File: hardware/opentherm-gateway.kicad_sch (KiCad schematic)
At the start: 83 parts, among them J1 BOILER, J2 THERM, J3 USB-C, J5 5V IN, J6 NTC, Q1 MMBT2907A, Q2 MMBT2907A, Q3 MMBT2907A, Q4 MMBT2907A, Q5 MMBT2222A, Q6 MMBT2222A, SW1 RESET, SW2 BOOT, U1 MT3540-F23, U2 LTV-817S, U3 LTV-817S, U4 ESP32-C3-WROOM-02-N4, U5 AP2112K-3.3, U6 USBLC6-2SC6

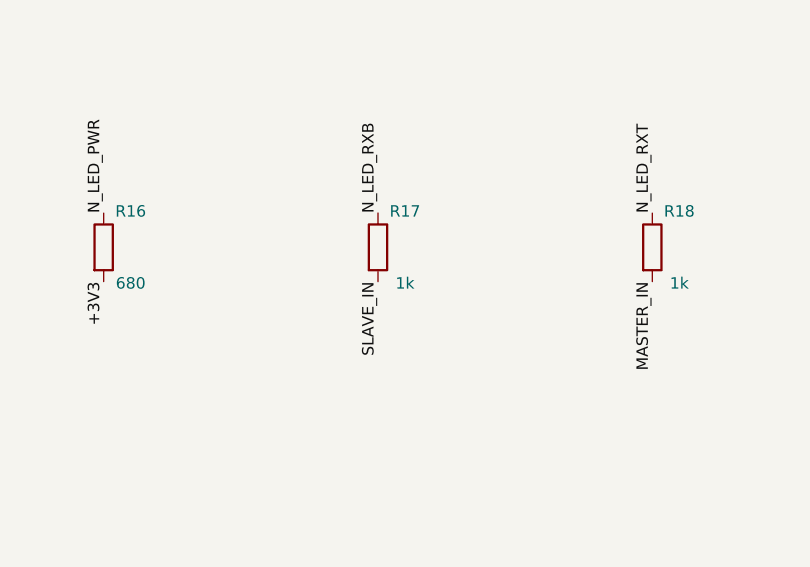
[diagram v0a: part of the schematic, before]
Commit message: hardware: complete BOM with LCSC part numbers (JLCPCB format too), fix ESP32 module code, R17 330R for the green LED
Co-Authored-By: Claude Sonnet 5.5 <noreply@anthropic.com>
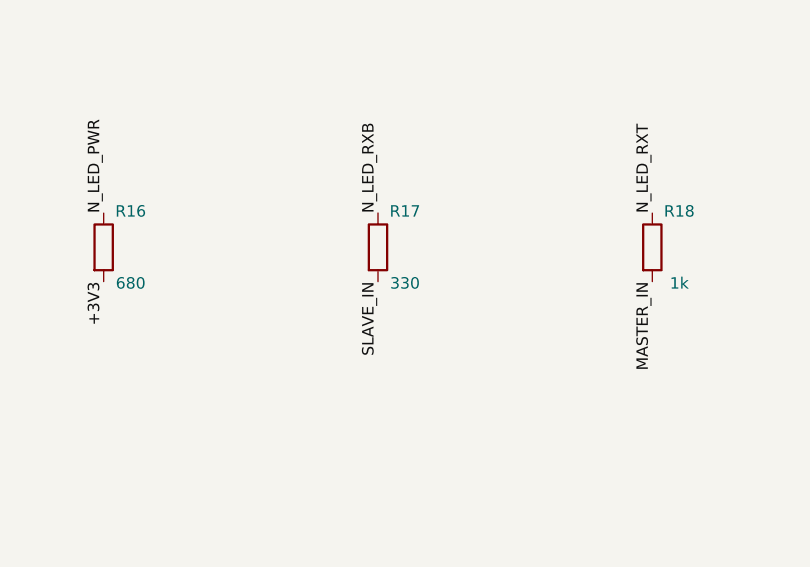
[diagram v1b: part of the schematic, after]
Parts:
- C1, C5: LCSC (none) -> C1713
- C2: LCSC (none) -> C1804
- C3, C6, C7: LCSC (none) -> C49678
- C8, C9: LCSC (none) -> C28323
- D15: LCSC (none) -> C84256
- D16, D17: LCSC (none) -> C113964
- J1, J2, J5, J6: LCSC (none) -> C474892
- R1: LCSC (none) -> C25824
- R10, R11: LCSC (none) -> C17544
- R12, R22, R23, R24, R25, R7: LCSC (none) -> C17414
- R13: LCSC (none) -> C17470
- R14, R18, R26: LCSC (none) -> C17513
- R15: LCSC (none) -> C17673
- R16: LCSC (none) -> C17798
- R17: value 1k -> 330; LCSC (none) -> C17630
- R19, R20: LCSC (none) -> C27834
- R2: LCSC (none) -> C17455
- R21: LCSC (none) -> C110775
- R3: LCSC (none) -> C17630
- R4: LCSC (none) -> C17557
- R5, R8: LCSC (none) -> C17408
- R6: LCSC (none) -> C28636
- R9: LCSC (none) -> C17633
- U4: LCSC C2934569 -> C2934560
